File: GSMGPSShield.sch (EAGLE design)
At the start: 66 parts, among them IC1 RT8289, IC2 C70710M0065002, IC3 SIM908, J1 Active GPS Antenna Bias, J2 M14, J5 ARDUINO-SHIELD_R3_NOISP, Q1 2N7002, Q2 RJU003N03 N-MOSFET, Q3 RJU003N03 N-MOSFET, Q4 RJU003N03 N-MOSFET, Q5 2N7002, Q6 2N7002, Q7 RJU003N03 N-MOSFET

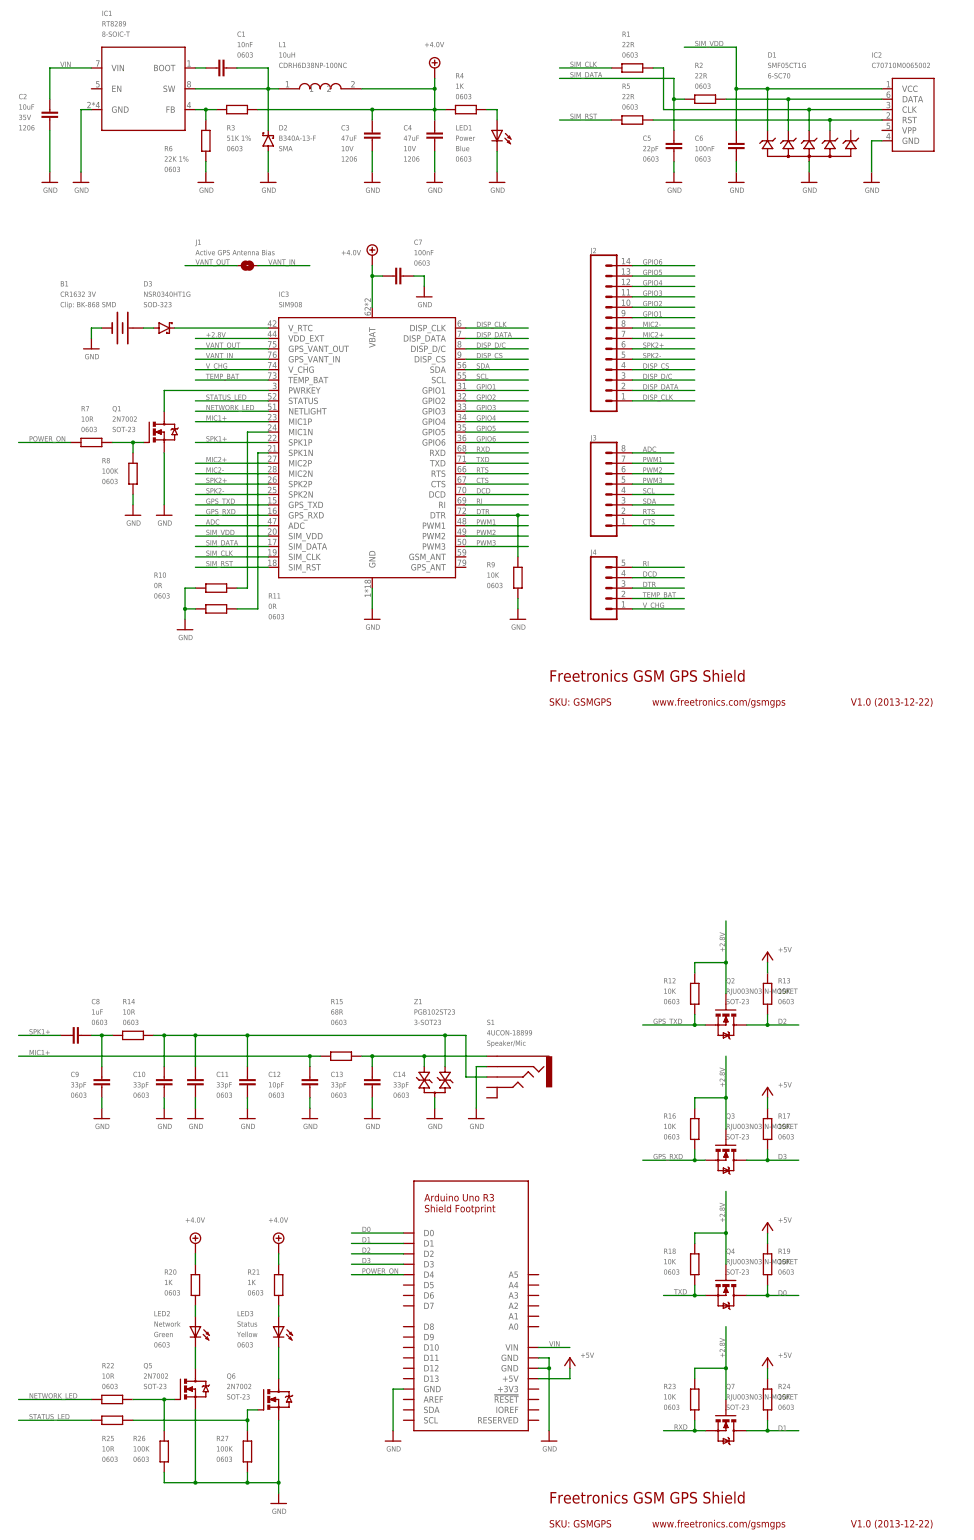
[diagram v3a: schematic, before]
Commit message: Fixed footprint for headphone socket Changed pin assignments to D2-D6 to clear D0/D1 UART for programming Added ICSP header for pass-through Replaced level shifter FETs with RJU003N03 Added orientation markers in tinfo layer for assembler Changed labels to vector and increased sizes
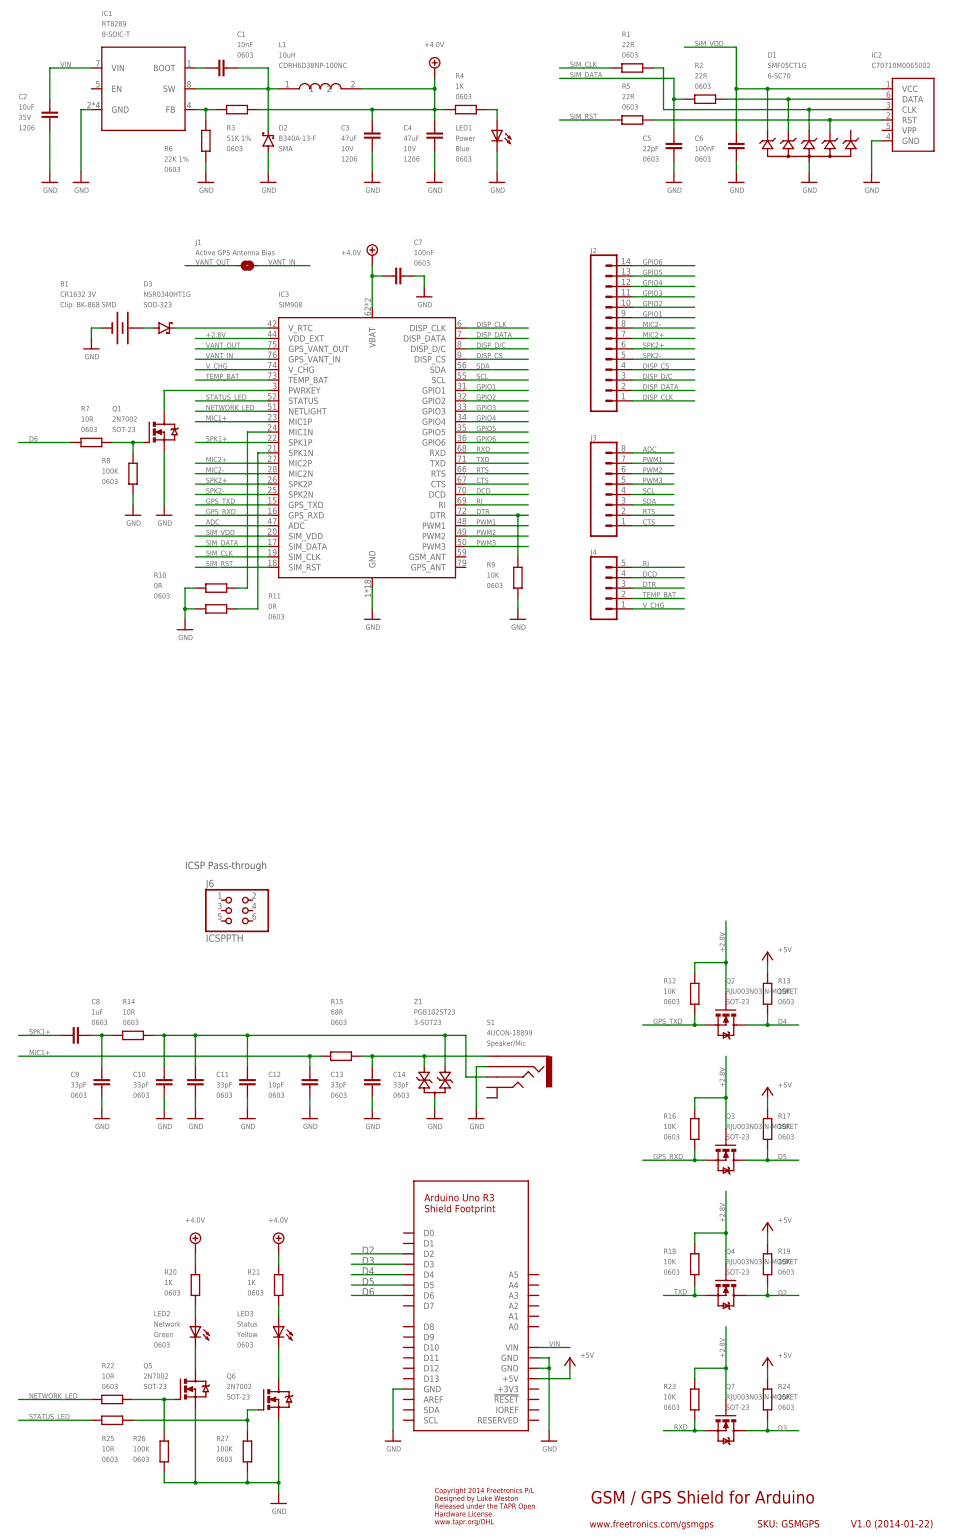
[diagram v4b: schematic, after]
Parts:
- added J6: ICSPPTH, freetronics-jon:ICSPPTH
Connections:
- removed net D0: J5.D0, Q4.D, R19.2
- removed net D1: J5.D1, Q7.D, R24.2
- removed net POWER_ON: J5.D4, R7.2
- new net D4: J5.D4, Q2.D, R13.2
- new net D5: J5.D5, Q3.D, R17.2
- new net D6: J5.D6, R7.2
- net D2: now also Q4.D, R19.2; no longer Q2.D, R13.2
- net D3: now also Q7.D, R24.2; no longer Q3.D, R17.2
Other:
- note added: "Copyright 2014 Freetronics P/L Designed by Luke Weston Released under the TAPR Open Hardware License www.tapr.org/OHL"
- note added: "GSM / GPS Shield for Arduino"
- note added: "ICSP Pass-through"
- note added: "V1.0 (2014-01-22)"
- note removed: "Freetronics GSM GPS Shield"
- note removed: "V1.0 (2013-12-22)"
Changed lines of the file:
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@@
 <layer number="111" name="LPC17xx" color="7" fill="1" visible="yes" active="yes"/>
 <layer number="112" name="tSilk" color="7" fill="1" visible="yes" active="yes"/>
+<layer number="113" name="ReferenceLS" color="7" fill="1" visible="yes" active="yes"/>
 <layer number="116" name="Patch_BOT" color="9" fill="4" visible="yes" active="yes"/>
 <layer number="118" name="Rect_Pads" color="7" fill="1" visible="yes" active="yes"/>
@@
 <part name="J5" library="freetronics-luke" deviceset="ARDUINO-SHIELD_R3_NOISP" device=""/>
 <part name="U$28" library="freetronics-luke" deviceset="+5V" device=""/>
+<part name="J6" library="freetronics-jon" deviceset="ICSP" device="PTH"/>
 </parts>
 <sheets>
 <sheet>
 <plain>
-<text x="142.24" y="213.36" size="2.794" layer="94">Freetronics GSM GPS Shield</text>
-<text x="215.9" y="207.518" size="1.778" layer="94">V1.0 (2013-12-22)</text>
-<text x="167.386" y="207.518" size="1.778" layer="94">www.freetronics.com/gsmgps</text>
-<text x="142.24" y="207.518" size="1.778" layer="94">SKU: GSMGPS</text>
 <frame x1="0" y1="200.66" x2="248.92" y2="386.08" columns="8" rows="5" layer="94"/>
-<frame x1="139.7" y1="205.74" x2="243.84" y2="218.44" columns="0" rows="0" layer="94" border-left="no" border-top="no" border-right="no" border-bottom="no"/>
-<frame x1="139.7" y1="205.74" x2="165.1" y2="210.82" columns="8" rows="5" layer="94"/>
-<frame x1="213.36" y1="205.74" x2="243.84" y2="210.82" columns="8" rows="5" layer="94"/>
 <wire x1="7.62" y1="325.12" x2="142.24" y2="325.12" width="0.1524" layer="98" style="shortdash"/>
 <wire x1="142.24" y1="325.12" x2="142.24" y2="220.98" width="0.1524" layer="98" style="shortdash"/>
@@
 <wire x1="83.82" y1="7.62" x2="7.62" y2="7.62" width="0.1524" layer="98" style="shortdash"/>
 <wire x1="7.62" y1="7.62" x2="7.62" y2="86.36" width="0.1524" layer="98" style="shortdash"/>
-<text x="142.24" y="12.7" size="2.794" layer="94">Freetronics GSM GPS Shield</text>
-<text x="142.24" y="6.858" size="1.778" layer="94">SKU: GSMGPS</text>
 <frame x1="0" y1="0" x2="248.92" y2="185.42" columns="8" rows="5" layer="94"/>
-<frame x1="139.7" y1="5.08" x2="243.84" y2="17.78" columns="0" rows="0" layer="94" border-left="no" border-top="no" border-right="no" border-bottom="no"/>
-<text x="215.9" y="6.858" size="1.778" layer="94">V1.0 (2013-12-22)</text>
-<text x="167.386" y="6.858" size="1.778" layer="94">www.freetronics.com/gsmgps</text>
-<frame x1="139.7" y1="5.08" x2="165.1" y2="10.16" columns="8" rows="5" layer="94"/>
-<frame x1="213.36" y1="5.08" x2="243.84" y2="10.16" columns="8" rows="5" layer="94"/>
 <wire x1="7.62" y1="101.6" x2="7.62" y2="139.7" width="0.1524" layer="98" style="shortdash"/>
 <wire x1="147.32" y1="139.7" x2="7.62" y2="139.7" width="0.1524" layer="98" style="shortdash"/>
@@
 <wire x1="208.28" y1="160.02" x2="208.28" y2="22.86" width="0.1524" layer="98" style="shortdash"/>
 <wire x1="160.02" y1="160.02" x2="208.28" y2="160.02" width="0.1524" layer="98" style="shortdash"/>
+<text x="152.4" y="12.7" size="3.048" layer="94">GSM / GPS Shield for Arduino</text>
+<text x="215.9" y="6.858" size="1.778" layer="94">V1.0 (2014-01-22)</text>
+<text x="152.146" y="6.858" size="1.651" layer="94">www.freetronics.com/gsmgps</text>
+<text x="193.04" y="6.858" size="1.778" layer="94">SKU: GSMGPS</text>
+<frame x1="149.86" y1="5.08" x2="243.84" y2="17.78" columns="0" rows="0" layer="94" border-left="no" border-top="no" border-right="no" border-bottom="no"/>
+<frame x1="190.5" y1="5.08" x2="213.36" y2="10.16" columns="8" rows="5" layer="94"/>
+<frame x1="213.36" y1="5.08" x2="243.84" y2="10.16" columns="8" rows="5" layer="94"/>
+<text x="114.3" y="7.62" size="1.27" layer="94">Copyright 2014 Freetronics P/L
+Designed by Luke Weston
+Released under the TAPR Open
+Hardware License
+www.tapr.org/OHL</text>
+<text x="53.34" y="167.64" size="1.778" layer="97">ICSP Pass-through</text>
 </plain>
 <instances>
@@
 <instance part="J5" gate="G$1" x="124.46" y="63.5"/>
 <instance part="U$28" gate="G$1" x="147.32" y="48.26"/>
+<instance part="J6" gate="G$1" x="66.04" y="157.48"/>
 </instances>
 <busses>
@@
 </segment>
 </net>
-<net name="POWER_ON" class="0">
+<net name="D4" class="0">
 <segment>
 <wire x1="106.68" y1="68.58" x2="93.98" y2="68.58" width="0.1524" layer="91"/>
-<label x="96.52" y="68.834" size="1.27" layer="95"/>
 <pinref part="J5" gate="G$1" pin="D4"/>
-</segment>
-<segment>
-<pinref part="R7" gate="G$1" pin="2"/>
-<wire x1="25.4" y1="271.78" x2="12.7" y2="271.78" width="0.1524" layer="91"/>
-<label x="15.24" y="272.034" size="1.27" layer="95"/>
+<label x="96.52" y="68.58" size="1.778" layer="95"/>
+</segment>
+<segment>
+<pinref part="Q2" gate="G$1" pin="D"/>
+<wire x1="190.5" y1="129.54" x2="195.58" y2="129.54" width="0.1524" layer="91"/>
+<pinref part="R13" gate="G$1" pin="2"/>
+<wire x1="195.58" y1="132.08" x2="195.58" y2="129.54" width="0.1524" layer="91"/>
+<wire x1="195.58" y1="129.54" x2="203.2" y2="129.54" width="0.1524" layer="91"/>
+<junction x="195.58" y="129.54"/>
+<label x="198.12" y="129.794" size="1.27" layer="95"/>
 </segment>
 </net>
@@
 </segment>
 </net>
-<net name="D0" class="0">
-<segment>
-<wire x1="93.98" y1="78.74" x2="106.68" y2="78.74" width="0.1524" layer="91"/>
-<label x="96.52" y="78.994" size="1.27" layer="95"/>
-<pinref part="J5" gate="G$1" pin="D0"/>
+<net name="D2" class="0">
+<segment>
+<wire x1="93.98" y1="73.66" x2="106.68" y2="73.66" width="0.1524" layer="91"/>
+<pinref part="J5" gate="G$1" pin="D2"/>
+<label x="96.52" y="73.66" size="1.778" layer="95"/>
 </segment>
 <segment>
@@
 </segment>
 </net>
-<net name="D2" class="0">
-<segment>
-<wire x1="93.98" y1="73.66" x2="106.68" y2="73.66" width="0.1524" layer="91"/>
-<label x="96.52" y="73.914" size="1.27" layer="95"/>
-<pinref part="J5" gate="G$1" pin="D2"/>
-</segment>
-<segment>
-<pinref part="Q2" gate="G$1" pin="D"/>
-<wire x1="190.5" y1="129.54" x2="195.58" y2="129.54" width="0.1524" layer="91"/>
-<pinref part="R13" gate="G$1" pin="2"/>
-<wire x1="195.58" y1="132.08" x2="195.58" y2="129.54" width="0.1524" layer="91"/>
-<wire x1="195.58" y1="129.54" x2="203.2" y2="129.54" width="0.1524" layer="91"/>
-<junction x="195.58" y="129.54"/>
-<label x="198.12" y="129.794" size="1.27" layer="95"/>
-</segment>
-</net>
-<net name="D1" class="0">
-<segment>
-<wire x1="93.98" y1="76.2" x2="106.68" y2="76.2" width="0.1524" layer="91"/>
-<label x="96.52" y="76.454" size="1.27" layer="95"/>
-<pinref part="J5" gate="G$1" pin="D1"/>
+<net name="D3" class="0">
+<segment>
+<wire x1="93.98" y1="71.12" x2="106.68" y2="71.12" width="0.1524" layer="91"/>
+<pinref part="J5" gate="G$1" pin="D3"/>
+<label x="96.52" y="71.12" size="1.778" layer="95"/>
 </segment>
 <segment>
@@
 <junction x="195.58" y="30.48"/>
 <label x="198.12" y="30.48" size="1.27" layer="95"/>
-</segment>
-</net>
-<net name="D3" class="0">
-<segment>
-<wire x1="93.98" y1="71.12" x2="106.68" y2="71.12" width="0.1524" layer="91"/>
-<label x="96.52" y="71.374" size="1.27" layer="95"/>
-<pinref part="J5" gate="G$1" pin="D3"/>
-</segment>
-<segment>
-<pinref part="Q3" gate="G$1" pin="D"/>
-<wire x1="190.5" y1="96.52" x2="195.58" y2="96.52" width="0.1524" layer="91"/>
-<pinref part="R17" gate="G$1" pin="2"/>
-<wire x1="195.58" y1="99.06" x2="195.58" y2="96.52" width="0.1524" layer="91"/>
-<wire x1="195.58" y1="96.52" x2="203.2" y2="96.52" width="0.1524" layer="91"/>
-<junction x="195.58" y="96.52"/>
-<label x="198.12" y="96.774" size="1.27" layer="95"/>
 </segment>
 </net>
@@
 </segment>
 </net>
+<net name="D5" class="0">
+<segment>
+<pinref part="J5" gate="G$1" pin="D5"/>
+<wire x1="106.68" y1="66.04" x2="93.98" y2="66.04" width="0.1524" layer="91"/>
+<label x="96.52" y="66.04" size="1.778" layer="95"/>
+</segment>
+<segment>
+<pinref part="Q3" gate="G$1" pin="D"/>
+<wire x1="190.5" y1="96.52" x2="195.58" y2="96.52" width="0.1524" layer="91"/>
+<pinref part="R17" gate="G$1" pin="2"/>
+<wire x1="195.58" y1="99.06" x2="195.58" y2="96.52" width="0.1524" layer="91"/>
+<wire x1="195.58" y1="96.52" x2="203.2" y2="96.52" width="0.1524" layer="91"/>
+<junction x="195.58" y="96.52"/>
+<label x="198.12" y="96.774" size="1.27" layer="95"/>
+</segment>
+</net>
+<net name="D6" class="0">
+<segment>
+<pinref part="J5" gate="G$1" pin="D6"/>
+<wire x1="106.68" y1="63.5" x2="93.98" y2="63.5" width="0.1524" layer="91"/>
+<label x="96.52" y="63.5" size="1.778" layer="95"/>
+</segment>
+<segment>
+<pinref part="R7" gate="G$1" pin="2"/>
+<wire x1="25.4" y1="271.78" x2="12.7" y2="271.78" width="0.1524" layer="91"/>
+<label x="15.24" y="272.034" size="1.27" layer="95"/>
+</segment>
+</net>
